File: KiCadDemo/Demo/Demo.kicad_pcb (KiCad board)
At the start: 4 copper layers, 100 x 80 mm, 66 parts, among them J1 Power, J2 22-05-7025, J3 22-05-7025, J4 22-05-7025, J5 22-05-7025, J6 Comm, J7 USB_B_Mini, J8 Debug, M1 BSS84, M2 BSS84, SW1 Reset, U1 TSR_1-2450, U2 UA78M33, U3 STM32F103CBT6, U4 DS1822-PAR, U5 MAX3486, U6 74LS06, X1 8 MHz

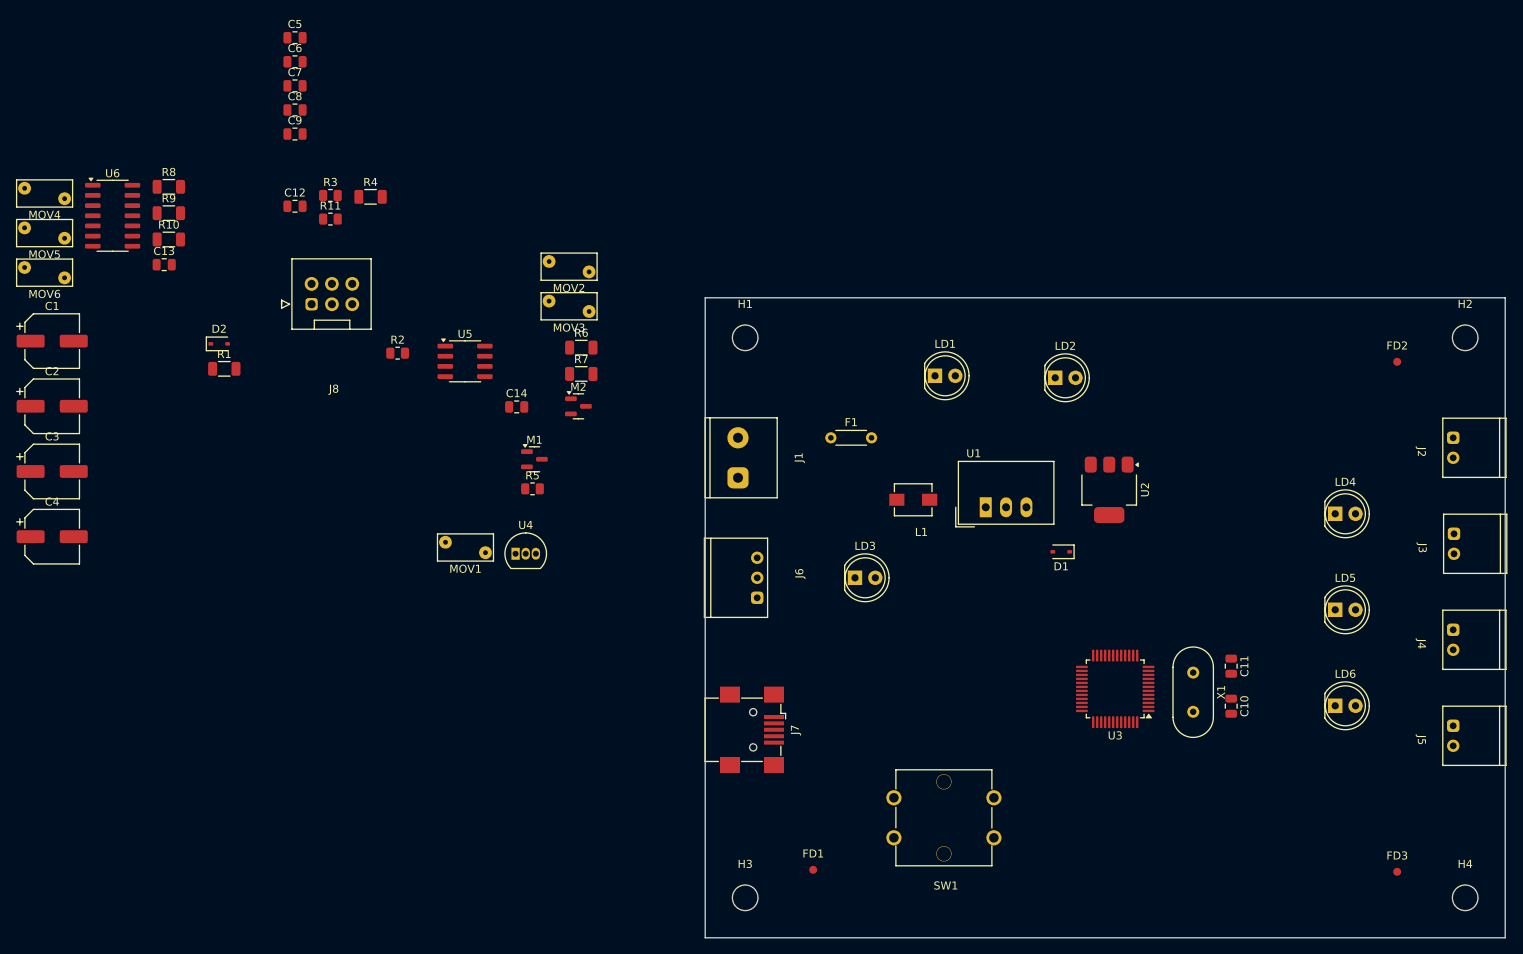
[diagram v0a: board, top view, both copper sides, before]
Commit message: Final placement version + fixed debug footprint
Final placement version + fixed debug footprint
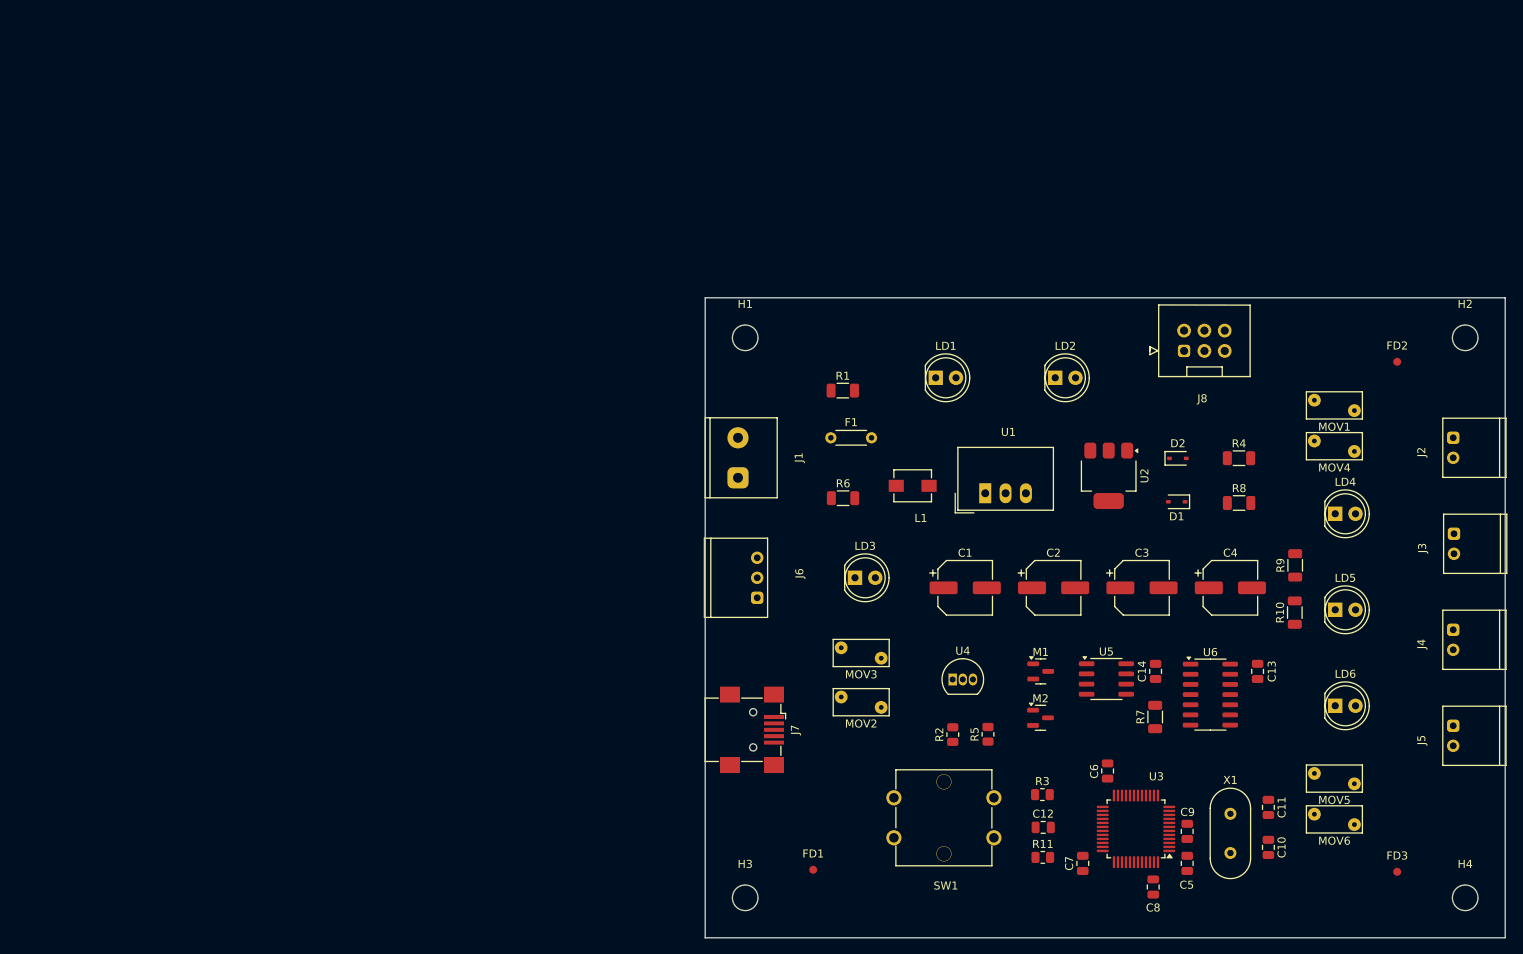
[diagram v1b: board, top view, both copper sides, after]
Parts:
- moved MOV6 175.1 mm to (176.2, 114.5)
- moved MOV5 175.1 mm to (176.2, 109.5)
- moved MOV4 164.3 mm to (176.2, 67.9)
- moved C5 152.0 mm to (160.2, 120.7), turned to 90 degrees
- moved U6 149.7 mm to (163.2, 99.6)
- moved R10 148.3 mm to (173.7, 89.3), turned to 90 degrees
- moved R9 147.5 mm to (173.8, 83.5), turned to 90 degrees
- moved C4 147.4 mm to (165.7, 86.2)
- moved C13 145.8 mm to (169.1, 96.7), turned to -90 degrees
- moved C8 144.7 mm to (156.0, 123.7), turned to 90 degrees
- moved C9 141.6 mm to (160.2, 116.7), turned to 90 degrees
- moved R8 139.5 mm to (166.7, 75.7)
- moved C7 138.4 mm to (147.2, 120.7), turned to 90 degrees
- moved C3 137.0 mm to (154.6, 86.2)
- moved C6 134.8 mm to (150.3, 109.2), turned to -90 degrees
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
